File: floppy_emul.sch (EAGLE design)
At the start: 25 parts, among them Q1 16MHz, U1 ATMEGA328P, U2 HEF4050B, U3 PCF8574T, U4 LM1117 3.3V

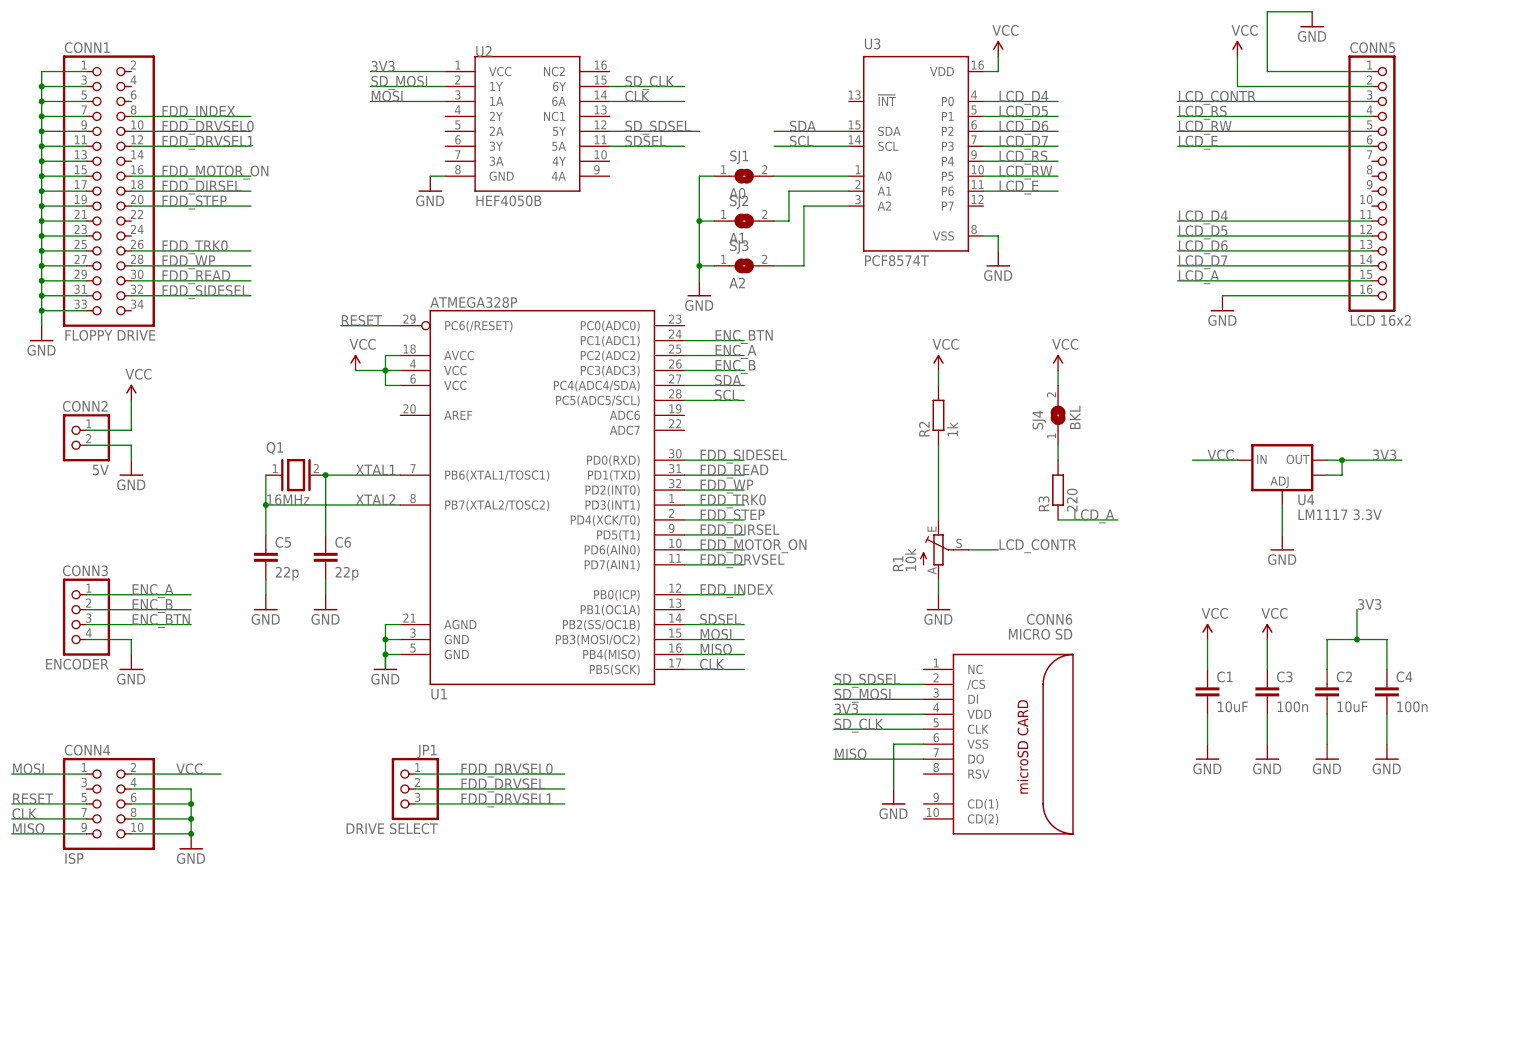
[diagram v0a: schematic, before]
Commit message: Changed SD card connector, added SPI connector for external SD module
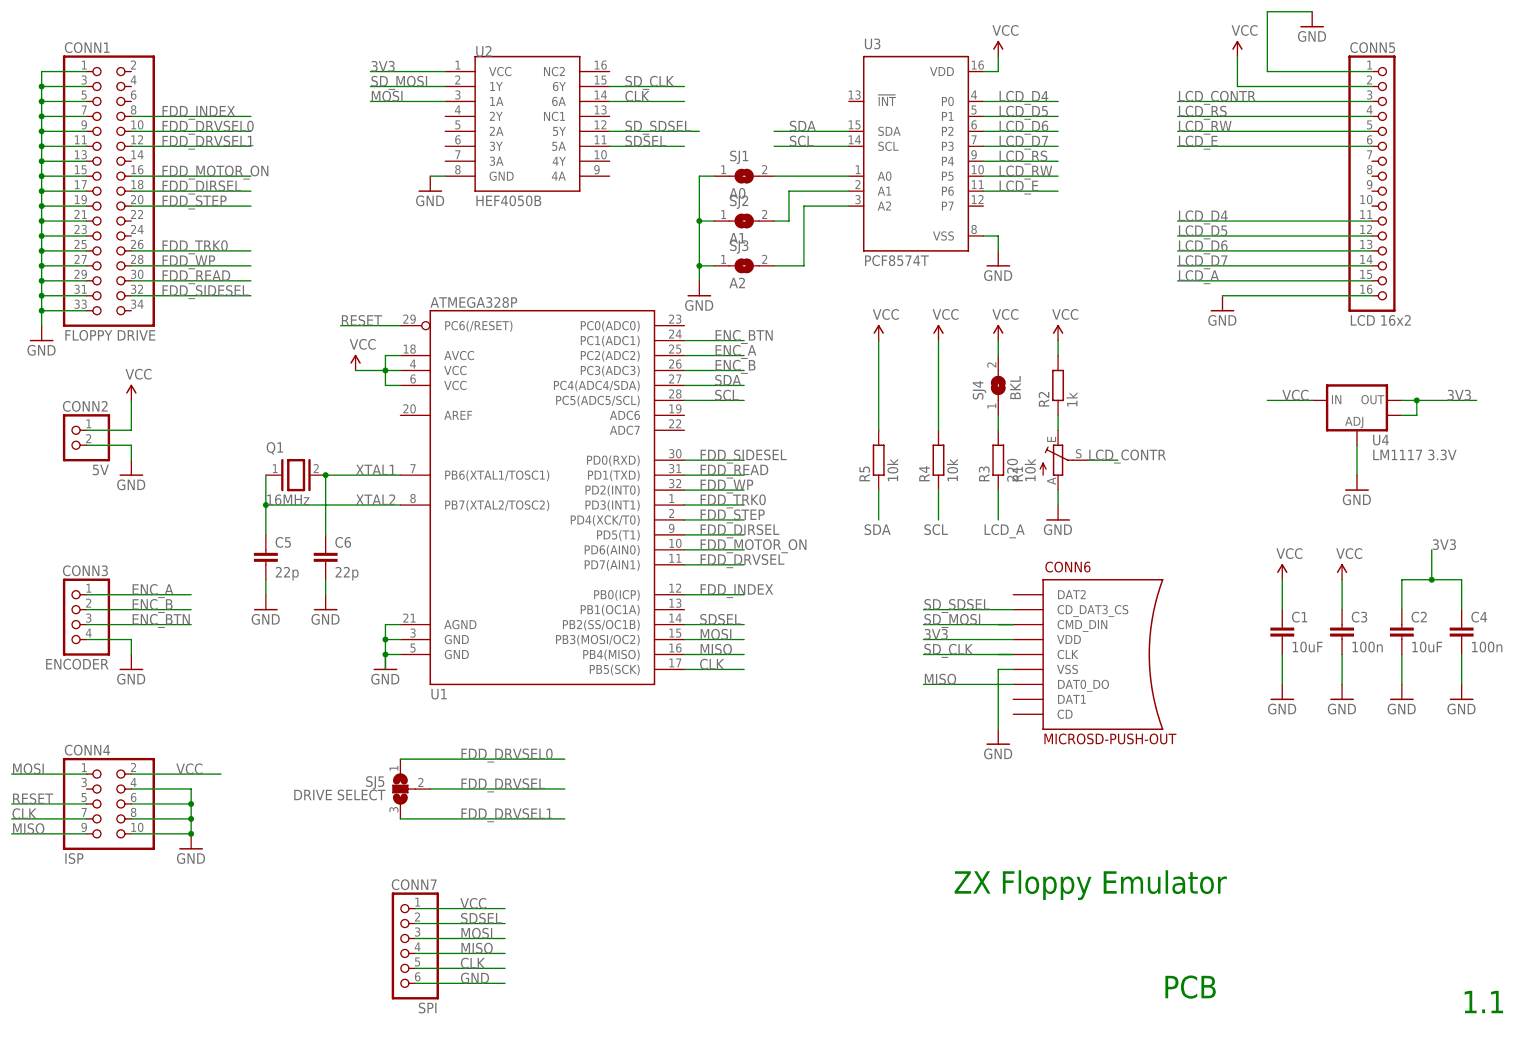
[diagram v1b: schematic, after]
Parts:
- removed JP1: DRIVE SELECT, pinhead:PINHD-1X3
- added CONN7: SPI, pinhead:PINHD-1X6
- added R4, R5: 10k, rcl:R-EU_R0805
- added SJ5: DRIVE SELECT, jumper:SJ2W
- CONN6: value MICRO SD -> MICROSD-PUSH-OUT; device con-molex-microsd:MICROSD_SPI_MODE -> microsd:MICROSD-PUSH-OUT
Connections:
- net CLK: now also CONN7.5
- net FDD_DRVSEL: now also SJ5.2; no longer JP1.2
- net FDD_DRVSEL0: now also SJ5.1; no longer JP1.1
- net FDD_DRVSEL1: now also SJ5.3; no longer JP1.3
- net GND: now also CONN7.6
- net MISO: now also CONN6.DAT0_DO, CONN7.4; no longer CONN6.DO
- net MOSI: now also CONN7.3
- net SCL: now also R4.1
- net SDA: now also R5.1
- net SDSEL: now also CONN7.2
- net SD_MOSI: now also CONN6.CMD_DIN; no longer CONN6.DI
- net SD_SDSEL: now also CONN6.CD_DAT3_CS; no longer CONN6./CS
- net VCC: now also CONN7.1, R4.2, R5.2
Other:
- note added: "1.1"
- note added: "PCB"
- note added: "ZX Floppy Emulator"
- moved on the sheet: C1, C2, C3, C4, R1, R2, R3, SJ4, U4

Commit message: board v1.2
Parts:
- removed CONN6: MICROSD-PUSH-OUT, microsd:MICROSD-PUSH-OUT
- removed CONN7: SPI, pinhead:PINHD-1X6
- removed SJ1: A0, jumper:SJ
- removed SJ2: A1, jumper:SJ
- removed SJ3: A2, jumper:SJ
- added J1: POWER_JACKPTH, SparkFun-Connectors:POWER_JACKPTH
- added JP1: EXT SD CARD, pinhead:PINHD-1X6
- added S1, S2, S3: (no value), switch-omron:10-XX
- added SD1: ST-TF-003A, Seeed-Connector:MICRO-SD-CARD-SOCKET-9P(ST-TF-003A)
- added SW1: ENCODER, piher:CI-11
- R1: device pot:TRIM_EU-CA6V -> pot:TRIM_EU-RJ9W
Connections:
- removed net N$3: SJ1.2, U3.A0
- removed net N$4: SJ2.2, U3.A1
- removed net N$5: SJ3.2, U3.A2
- new net LCD_LIGHT: U3.P3
- net 3V3: now also JP1.3, SD1.VDD; no longer CONN6.VDD
- net CLK: no longer CONN7.5
- net ENC_A: now also S1.S, S1.S1, SW1A.A
- net ENC_B: now also S3.S, S3.S1, SW1A.B
- net ENC_BTN: now also S2.S, S2.S1, SW1B.D
- net GND: now also J1.GND, J1.GNDBREAK, JP1.5, S1.P, S1.P1, S2.P, S2.P1, S3.P, S3.P1, SD1.G1, SD1.G2, SD1.G3, SD1.G4, SD1.VSS, SW1A.C, SW1B.E, U3.A0, U3.A1, U3.A2; no longer CONN6.VSS, CONN7.6, SJ1.1, SJ2.1, SJ3.1
- net LCD_D4: now also U3.P4; no longer U3.P0
- net LCD_D5: now also U3.P5; no longer U3.P1
- net LCD_D6: now also U3.P6; no longer U3.P2
- net LCD_D7: now also U3.P7; no longer U3.P3
- net LCD_E: now also U3.P2; no longer U3.P6
- net LCD_RS: now also U3.P0; no longer U3.P4
- net LCD_RW: now also U3.P1; no longer U3.P5
- net MISO: now also JP1.6, SD1.DO; no longer CONN6.DAT0_DO, CONN7.4
- net MOSI: no longer CONN7.3
- net SDSEL: no longer CONN7.2
- net SD_CLK: now also JP1.4, SD1.SCLK; no longer CONN6.CLK
- net SD_MOSI: now also JP1.2, SD1.DI; no longer CONN6.CMD_DIN
- net SD_SDSEL: now also JP1.1, SD1.CS; no longer CONN6.CD_DAT3_CS
- net VCC: now also J1.PWR; no longer CONN7.1
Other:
- note added: "1.2"
- note removed: "1.1"
- moved on the sheet: C1, C2, C3, C4

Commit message: new pcb revision: fixed encoder connections, small improvements
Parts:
- J1: value POWER_JACKPTH -> DC 5V; device SparkFun-Connectors:POWER_JACKPTH -> con-jack:JACK-PLUG0
- S1: value (none) -> A
- S2: value (none) -> SEL
- S3: value (none) -> B
- SW1: value ENCODER -> EC12E_SW; device piher:CI-11 -> switch-alps-mod:EC12E_SW
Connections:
- net ENC_A: now also SW1G$1.A; no longer SW1A.A
- net ENC_B: now also SW1G$1.B; no longer SW1A.B
- net ENC_BTN: now also SW1G$2.1; no longer SW1B.D
- net GND: now also J1.1, J1.2, SW1G$1.C, SW1G$2.2; no longer J1.GND, J1.GNDBREAK, SW1A.C, SW1B.E
- net VCC: now also J1.3; no longer J1.PWR
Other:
- note added: "1.2a"
- note removed: "1.2"
